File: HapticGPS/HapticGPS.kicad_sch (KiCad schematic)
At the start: 18 parts, among them J1 Conn_01x04

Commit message: updating
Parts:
- removed C1, C2, C5: 10uF, symbol Device:C
- removed C3: 2.2uF, symbol Device:C
- removed C4, C6: 100nF, symbol Device:C
- removed C7: 1uF, symbol Device:C
- removed J1: Conn_01x04, symbol Connector_Generic:Conn_01x04
- removed L1, L2: L, symbol Device:L
- removed R1, R2, R3, R6, R7: R, symbol Device:R
- removed R4, R5: 100K, symbol Device:R
- removed U1: ~, Package_DFN_QFN:VQFN-32-1EP_5x5mm_P0.5mm_EP3.1x3.1mm_ThermalVias, symbol Sadman_power:NPM1300
- added J1: Conn_01x05, symbol Connector_Generic:Conn_01x05
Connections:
- net +5V: now also J1.5 (Pin_5)
- net GND: now also J1.1 (Pin_1)
- new net NRF_RESET: J1.2 (Pin_2)
- new net NRF_SWDCLK: J1.4 (Pin_4)
- new net NRF_SWDIO: J1.3 (Pin_3)
- no-connect marks 9 -> 1
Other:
- added sheet CONTROLLER (modules/controller.sch.kicad_sch)
- added sheet GPS_INTERFACE (./modules/gps_interface.kicad_sch)
- added sheet PIEZOELECTRIC DRIVER (modules/piezoelectric_driver.kicad_sch)
- added sheet PIEZOELECTRIC DRIVER 2 (modules/piezoelectric_driver_2.sch.kicad_sch)
- added sheet POWER (modules/power.kicad_sch)
- note added: "CONTROLLER-NRF54L15"
- note added: "GPS INTERFACE"
- note added: "PMIC-NPM1300"
- note added: "PZ DRIVER TEST 1"
- note added: "PZ DRIVER TEST 2"

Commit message: save
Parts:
- added J5: Conn_01x10, Connector_FFC-FPC:Amphenol_F32Q-1A7x1-11010_1x10-1MP_P0.5mm_Horizontal, symbol Connector_Generic:Conn_01x10
- added R22: 1k, Resistor_SMD:R_0603_1608Metric, symbol Device:R
- added U7: TPS22917DBV, Package_TO_SOT_SMD:SOT-23-6, symbol Power_Management:TPS22917DBV
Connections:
- net GND: now also J5.2 (Pin_2), U7.2 (GND)
- new net: R22.1, U7.5 (QOD)
- new net +3VDC1: U7.1 (VIN), U7.4 (CT)
- new net CTRL_GPS: U7.3 (ON)
- new net GPS_NRST: J5.5 (Pin_5)
- new net GPS_RX: J5.3 (Pin_3)
- new net GPS_TX: J5.4 (Pin_4)
- new net GPS_WK: J5.6 (Pin_6)
- new net IMU_INT1: J5.9 (Pin_9)
- new net IMU_INT2: J5.10 (Pin_10)
- new net SCL_OUT: J5.8 (Pin_8)
- new net SDA_OUT: J5.7 (Pin_7)
- new net VINC_GPS: J5.1 (Pin_1), R22.2, U7.6 (VOUT)
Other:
- added sheet IMU (.modules/imu.kicad_sch)
- sheet CONTROLLER ports: added NRF_VIN; removed none
- sheet GPS_INTERFACE ports: added CTRL_GPS, NRST_GPS, RX_GPS, TX_GPS, VIN_GPS, WKUP_GPS; removed none
- note added: "IMU"

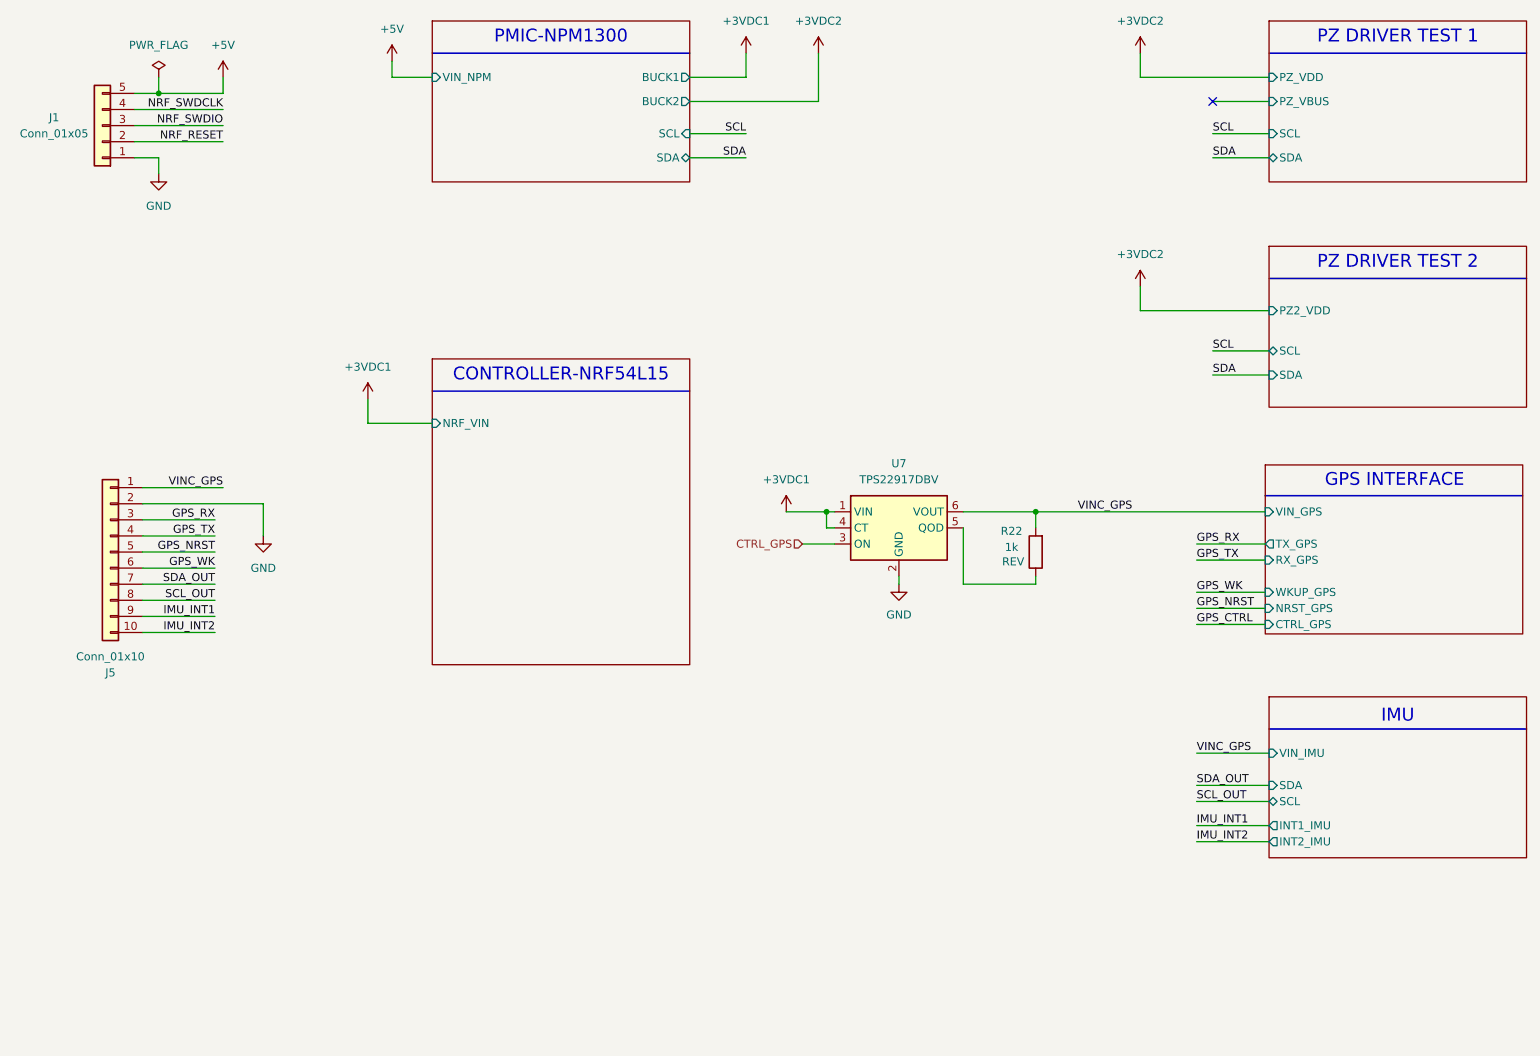
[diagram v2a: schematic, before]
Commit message: eliminating GPS, and second piezo driver
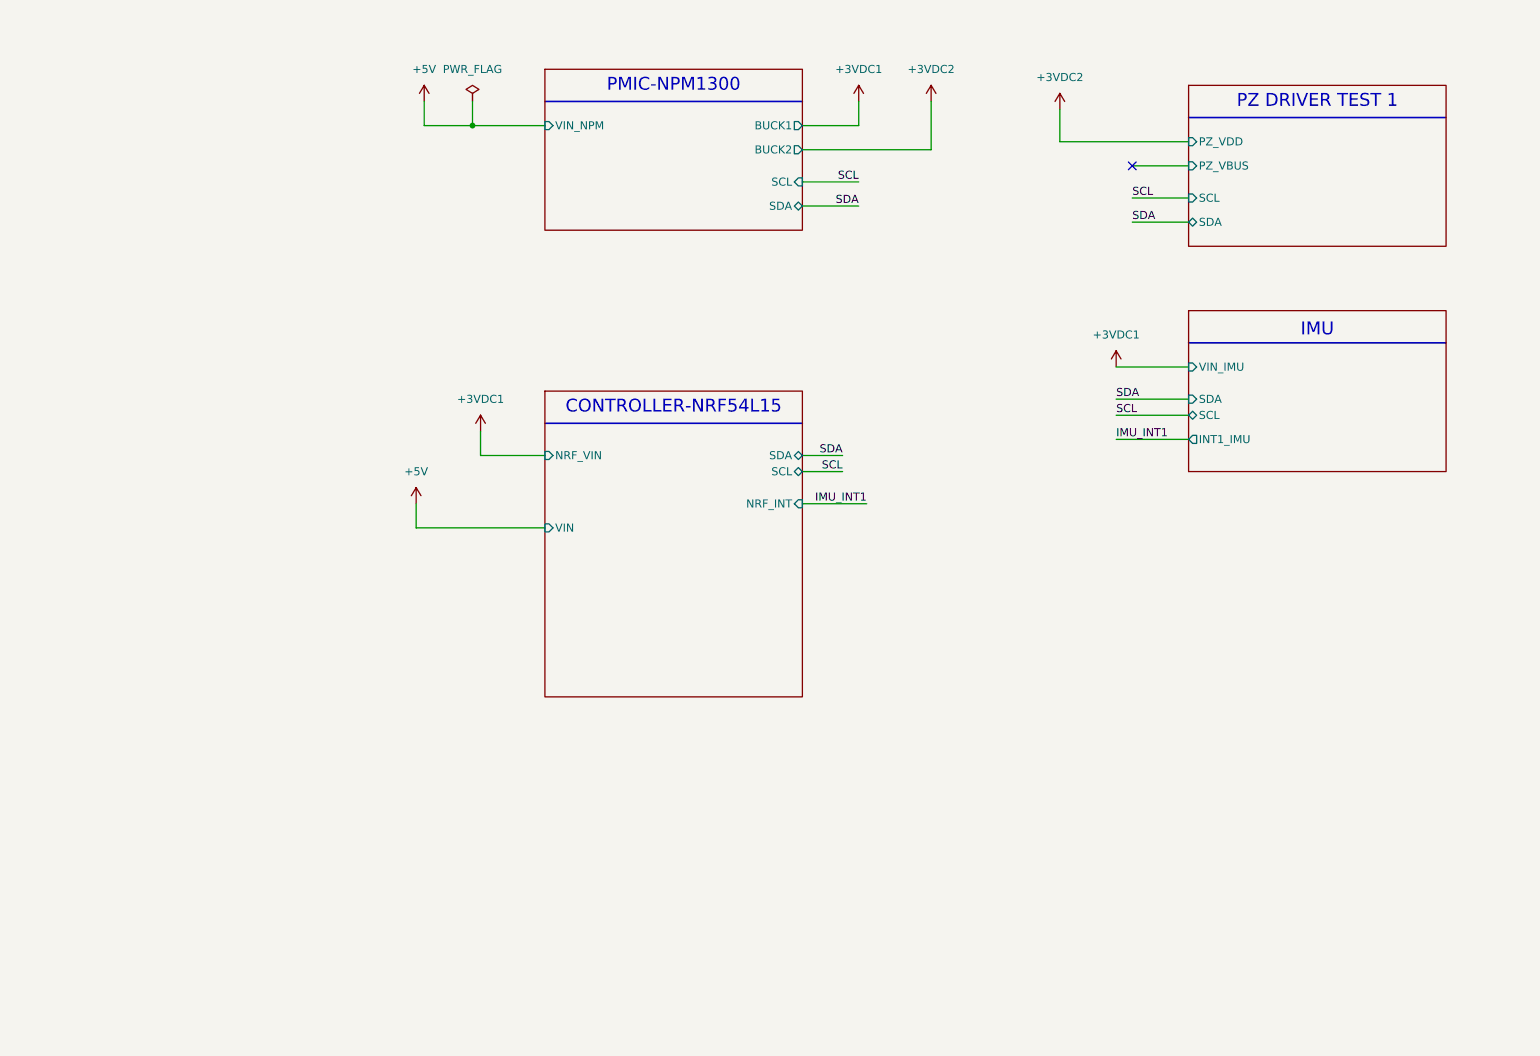
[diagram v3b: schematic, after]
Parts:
- removed J1: Conn_01x05, symbol Connector_Generic:Conn_01x05
- removed J5: Conn_01x10, Connector_FFC-FPC:Amphenol_F32Q-1A7x1-11010_1x10-1MP_P0.5mm_Horizontal, symbol Connector_Generic:Conn_01x10
- removed R22: 1k, Resistor_SMD:R_0603_1608Metric, symbol Device:R
- removed U7: TPS22917DBV, Package_TO_SOT_SMD:SOT-23-6, symbol Power_Management:TPS22917DBV
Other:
- removed sheet GPS_INTERFACE
- removed sheet PIEZOELECTRIC DRIVER 2
- sheet CONTROLLER ports: added NRF_INT, SCL, SDA, VIN; removed none
- sheet IMU ports: added none; removed INT2_IMU
- note removed: "GPS INTERFACE"
- note removed: "PZ DRIVER TEST 2"
